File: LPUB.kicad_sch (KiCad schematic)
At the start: 30 parts, among them IC1 ATMEGA324PA-AU, J1 Conn_01x06_Pin, J2 AVR-ISP-6, J3 Conn_02x10_Odd_Even, SW1 SW_MEC_5G, U1 LAMBDA80 (SX1280), U2 MB85RS64T, U4 LP2950-3.0_TO252, Y1 Crystal_GND24

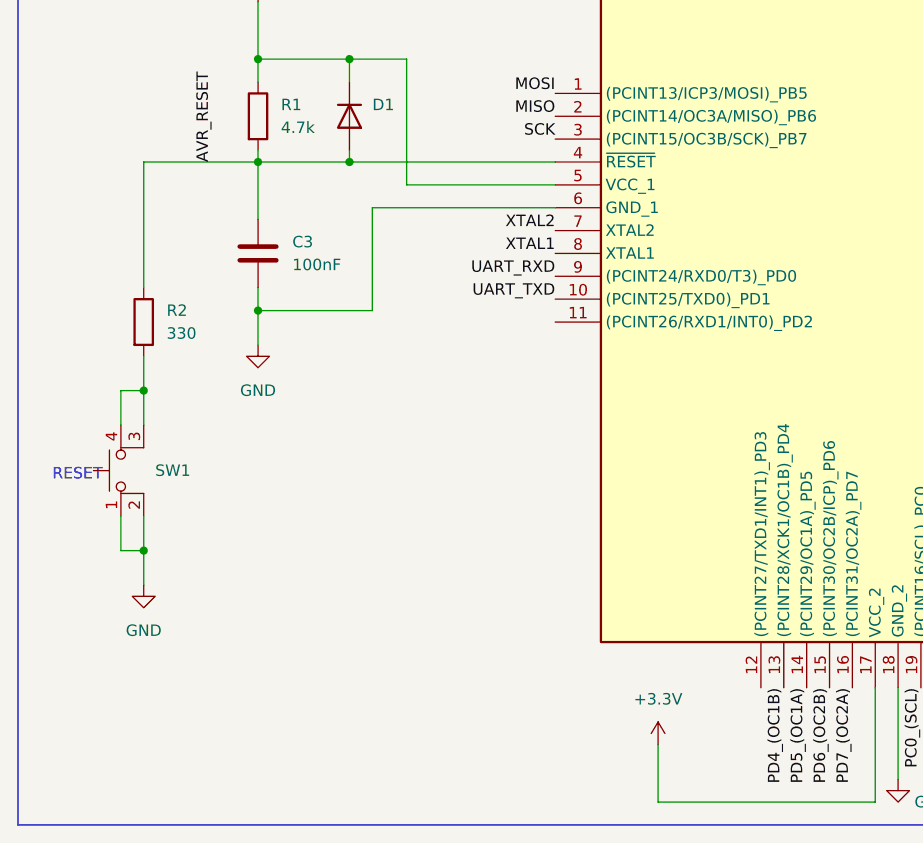
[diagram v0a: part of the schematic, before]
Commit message: added Button A and B to schematic
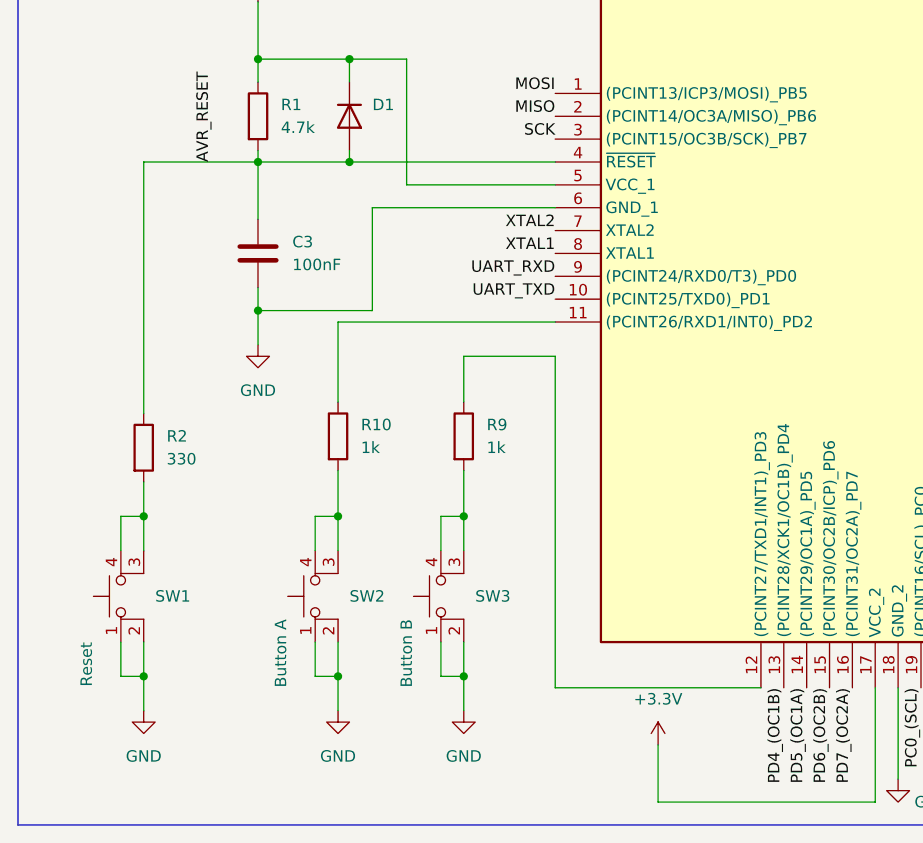
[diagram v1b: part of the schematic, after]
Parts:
- added R10, R9: 1k, Resistor_SMD:R_0805_2012Metric, symbol Device:R
- added SW2: Button A, DISCO_footprints:SW_Push_1P1T_NO_6x6mm_H9.5mm, symbol Switch:SW_MEC_5E
- added SW3: Button B, DISCO_footprints:SW_Push_1P1T_NO_6x6mm_H9.5mm, symbol Switch:SW_MEC_5E
- SW1: value SW_MEC_5G -> Reset
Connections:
- net GND: now also SW2.1, SW2.2, SW3.1, SW3.2
- net at IC1.11 ((PCINT26/RXD1/INT0)_PD2): now also R10.1
- net at IC1.12 ((PCINT27/TXD1/INT1)_PD3): now also R9.1
- new net: R9.2, SW3.3 (K), SW3.4 (A)
- new net: R10.2, SW2.3 (K), SW2.4 (A)
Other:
- note removed: "RESET"
- moved on the sheet: R2, SW1
